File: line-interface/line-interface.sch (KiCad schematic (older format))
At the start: 25 parts

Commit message: Source transil
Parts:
- D?: footprint (none) -> Diodes_SMD:DO-214AB; Distributor (none) -> 9381830; Manufacturer (none) -> MULTICOMP; PartNo (none) -> 1.5SMCJ48CA
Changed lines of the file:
@@
 F 0 "D?" V 1154 1829 50  0000 L CNN
 F 1 "D_TVS_ALT" V 1245 1829 50  0000 L CNN
-F 2 "" H -550 350 50  0001 C CNN
+F 2 "Diodes_SMD:DO-214AB" H -550 350 50  0001 C CNN
 F 3 "" H -550 350 50  0001 C CNN
+F 4 "1.5SMCJ48CA" H 1200 1750 60  0001 C CNN "PartNo"
+F 5 "MULTICOMP" H 1200 1750 60  0001 C CNN "Manufacturer"
+F 6 "9381830" H 1200 1750 60  0001 C CNN "Distributor"
 	1    1200 1750
 	0    1    1    0

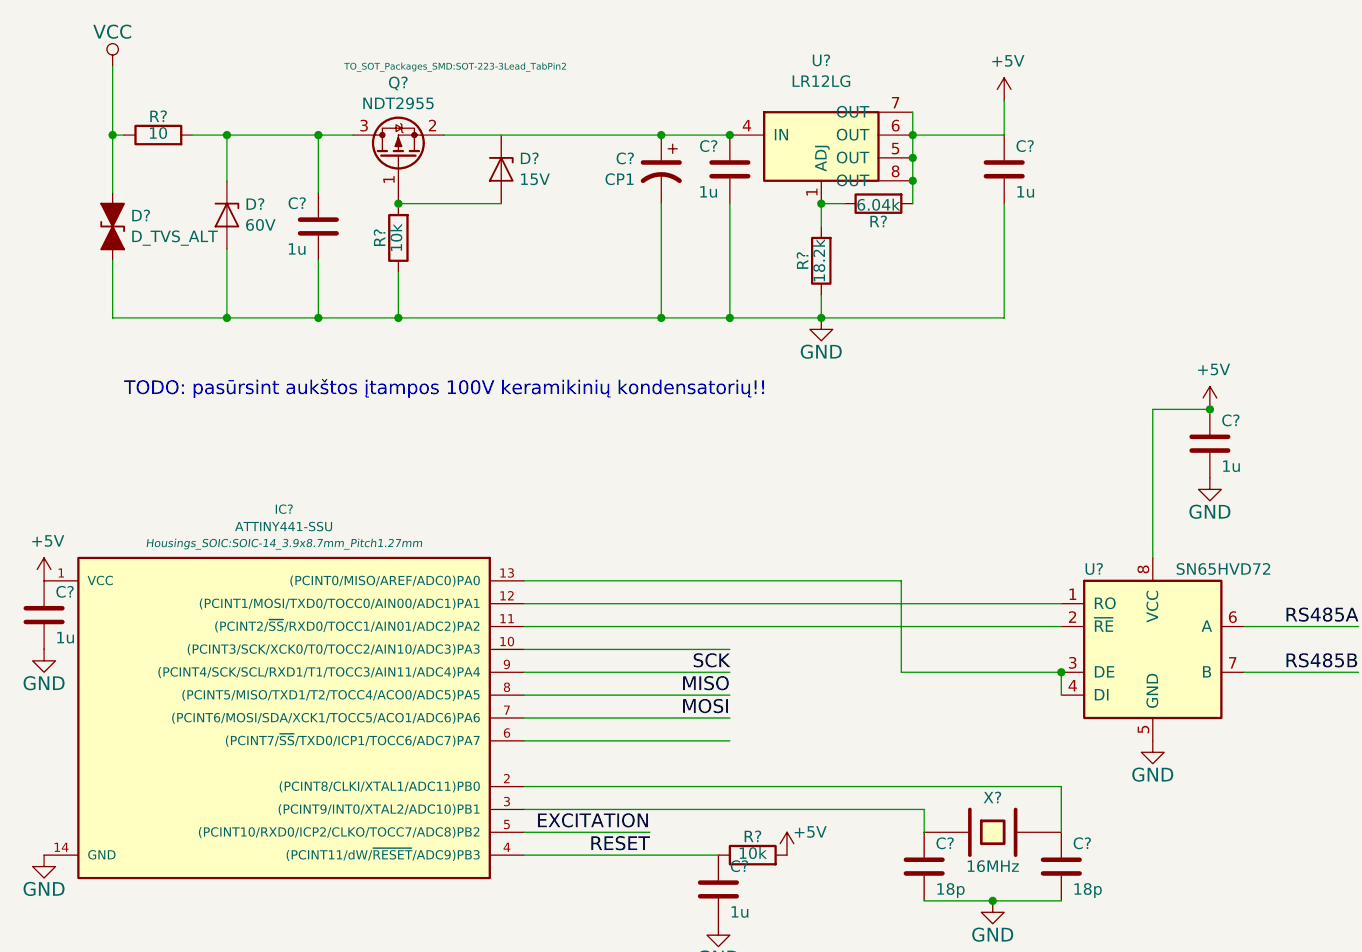
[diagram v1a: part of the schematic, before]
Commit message: Add more leds
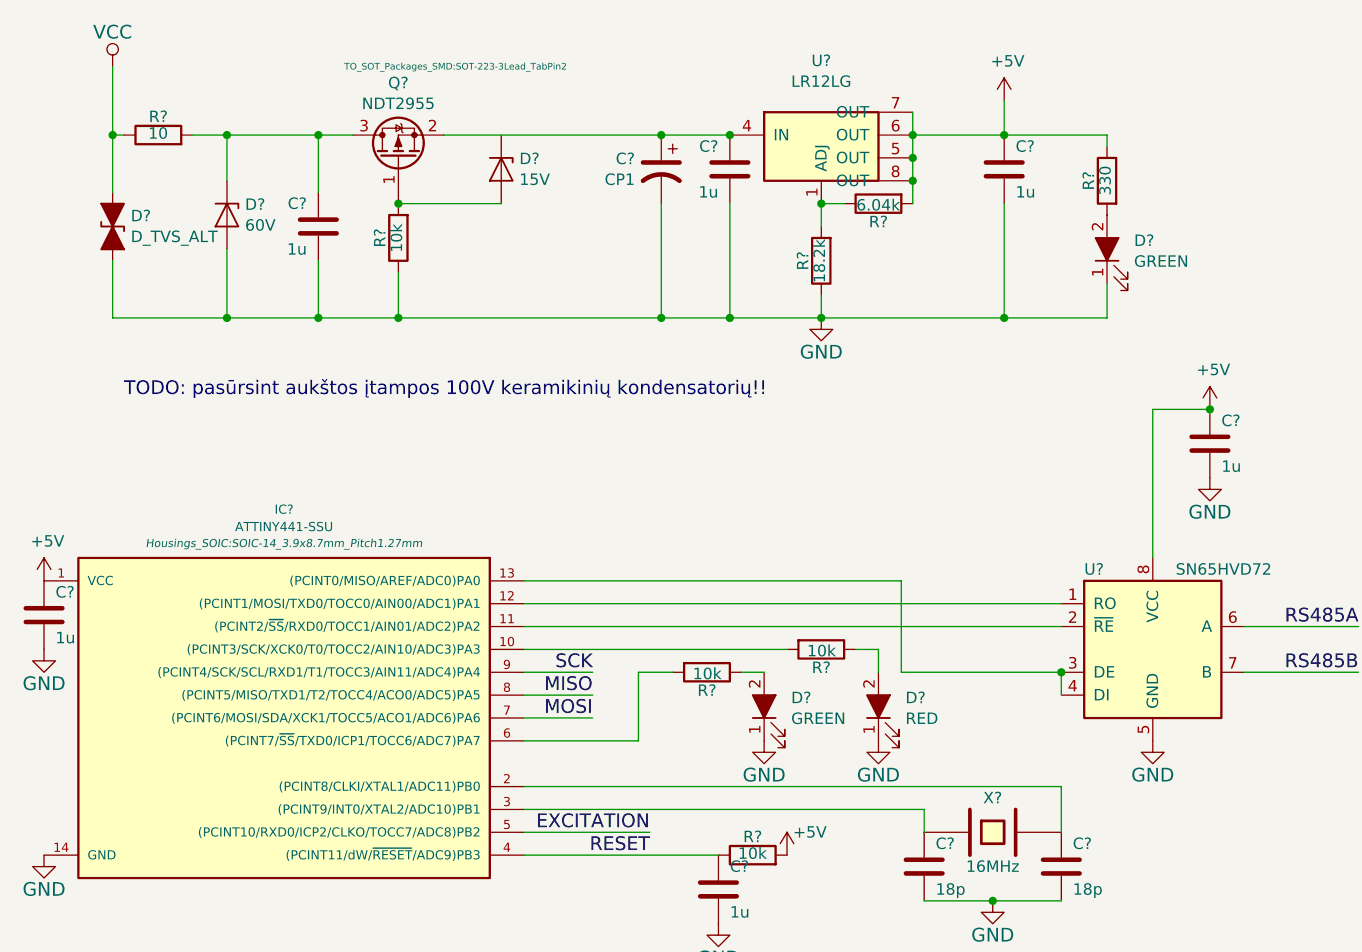
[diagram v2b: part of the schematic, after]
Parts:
- added D? (x2): GREEN, LEDs:LED_0603, symbol LED_ALT
- added D?: RED, LEDs:LED_0603, symbol LED_ALT
- added R?: 330, Resistors_SMD:R_0603, symbol R
- added R? (x2): 10k, Resistors_SMD:R_0603, symbol R
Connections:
- wire segments 57 -> 64
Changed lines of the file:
@@
 	1    0    0    -1
 $EndComp
-Text Label 3900 3700 2    60   ~ 0
+Text Label 3300 3700 2    60   ~ 0
 SCK
 Text Label 3550 4500 2    60   ~ 0
@@
 Text Label 3550 4400 2    60   ~ 0
 EXCITATION
-Text Label 3900 3800 2    60   ~ 0
+Text Label 3300 3800 2    60   ~ 0
 MISO
 Text Label 6650 3500 2    60   ~ 0
@@
 	3000 4400 3550 4400
 Wire Wire Line
-	3000 3800 3900 3800
-Wire Wire Line
-	3000 4000 3900 4000
+	3000 3800 3300 3800
+Wire Wire Line
+	3000 4000 3500 4000
 Wire Wire Line
 	6150 3500 6650 3500
@@
 	4650 3300 3000 3300
 Wire Wire Line
-	3900 3700 3000 3700
-Wire Wire Line
-	3000 3600 3900 3600
+	3300 3700 3000 3700
 $Comp
 L CONN_02X03 P?
@@
 $EndComp
 Wire Wire Line
-	4700 1350 5100 1350
+	4700 1350 5550 1350
 Connection ~ 4300 2150
 Wire Wire Line
@@
 	6150 3700 6650 3700
 Wire Wire Line
-	1200 2150 5100 2150
+	1200 2150 5550 2150
 Wire Wire Line
 	3900 1650 3900 2150
@@
 $EndComp
 Wire Wire Line
-	3000 3900 3900 3900
-Text Label 3900 3900 2    60   ~ 0
+	3000 3900 3300 3900
+Text Label 3300 3900 2    60   ~ 0
 MOSI
 $Comp
@@
 	2100 1600 2100 1350
 Connection ~ 2100 1350
+$Comp
+L LED_ALT D?
+U 1 1 58BD3E84
+P 4050 3850
+F 0 "D?" V 4088 3732 50  0000 R CNN
+F 1 "GREEN" V 3997 3732 50  0000 R CNN
+F 2 "LEDs:LED_0603" H -100 200 50  0001 C CNN
+F 3 "" H -100 200 50  0001 C CNN
+F 4 "?" H 4050 3850 60  0001 C CNN "PartNo"
+F 5 "?" H 4050 3850 60  0001 C CNN "Manufacturer"
+F 6 "?" H 4050 3850 60  0001 C CNN "Distributor"
+	1    4050 3850
+	0    -1   -1   0
+$EndComp
+$Comp
+L LED_ALT D?
+U 1 1 58BD44C6
+P 4550 3850
+F 0 "D?" V 4588 3732 50  0000 R CNN
+F 1 "RED" V 4497 3732 50  0000 R CNN
+F 2 "LEDs:LED_0603" H 400 200 50  0001 C CNN
+F 3 "" H 400 200 50  0001 C CNN
+F 4 "?" H 4550 3850 60  0001 C CNN "PartNo"
+F 5 "?" H 4550 3850 60  0001 C CNN "Manufacturer"
+F 6 "?" H 4550 3850 60  0001 C CNN "Distributor"
+	1    4550 3850
+	0    -1   -1   0
+$EndComp
+Wire Wire Line
+	4550 3600 4550 3700
+Wire Wire Line
+	3500 4000 3500 3700
+$Comp
+L GND #PWR?
+U 1 1 58BD465C
+P 4050 4000
+F 0 "#PWR?" H 4050 3750 60  0001 C CNN
+F 1 "GND" H 4050 3850 60  0000 C CNN
+F 2 "" H 4050 4000 60  0000 C CNN
+F 3 "" H 4050 4000 60  0000 C CNN
+	1    4050 4000
+	1    0    0    -1
+$EndComp
+$Comp
+L GND #PWR?
+U 1 1 58BD4709
+P 4550 4000
+F 0 "#PWR?" H 4550 3750 60  0001 C CNN
+F 1 "GND" H 4550 3850 60  0000 C CNN
+F 2 "" H 4550 4000 60  0000 C CNN
+F 3 "" H 4550 4000 60  0000 C CNN
+	1    4550 4000
+	1    0    0    -1
+$EndComp
+$Comp
+L LED_ALT D?
+U 1 1 58BD48E7
+P 5550 1850
+F 0 "D?" V 5588 1732 50  0000 R CNN
+F 1 "GREEN" V 5497 1732 50  0000 R CNN
+F 2 "LEDs:LED_0603" H 1400 -1800 50  0001 C CNN
+F 3 "" H 1400 -1800 50  0001 C CNN
+F 4 "?" H 5550 1850 60  0001 C CNN "PartNo"
+F 5 "?" H 5550 1850 60  0001 C CNN "Manufacturer"
+F 6 "?" H 5550 1850 60  0001 C CNN "Distributor"
+	1    5550 1850
+	0    -1   -1   0
+$EndComp
+Wire Wire Line
+	5550 2150 5550 2000
+Connection ~ 5100 2150
+$Comp
+L R R?
+U 1 1 58BD4C42
+P 5550 1550
+F 0 "R?" V 5630 1550 50  0000 C CNN
+F 1 "330" V 5557 1551 50  0000 C CNN
+F 2 "Resistors_SMD:R_0603" V 5480 1550 30  0001 C CNN
+F 3 "" H 5550 1550 30  0000 C CNN
+	1    5550 1550
+	-1   0    0    -1
+$EndComp
+Connection ~ 5100 1350
+Wire Wire Line
+	5550 1350 5550 1400
+$Comp
+L R R?
+U 1 1 58BD52D2
+P 4300 3600
+F 0 "R?" V 4380 3600 50  0000 C CNN
+F 1 "10k" V 4307 3601 50  0000 C CNN
+F 2 "Resistors_SMD:R_0603" V 4230 3600 30  0001 C CNN
+F 3 "" H 4300 3600 30  0000 C CNN
+	1    4300 3600
+	0    1    1    0
+$EndComp
+$Comp
+L R R?
+U 1 1 58BD5396
+P 3800 3700
+F 0 "R?" V 3880 3700 50  0000 C CNN
+F 1 "10k" V 3807 3701 50  0000 C CNN
+F 2 "Resistors_SMD:R_0603" V 3730 3700 30  0001 C CNN
+F 3 "" H 3800 3700 30  0000 C CNN
+	1    3800 3700
+	0    1    1    0
+$EndComp
+Wire Wire Line
+	3000 3600 4150 3600
+Wire Wire Line
+	4450 3600 4550 3600
+Wire Wire Line
+	3950 3700 4050 3700
+Wire Wire Line
+	3500 3700 3650 3700
 $EndSCHEMATC

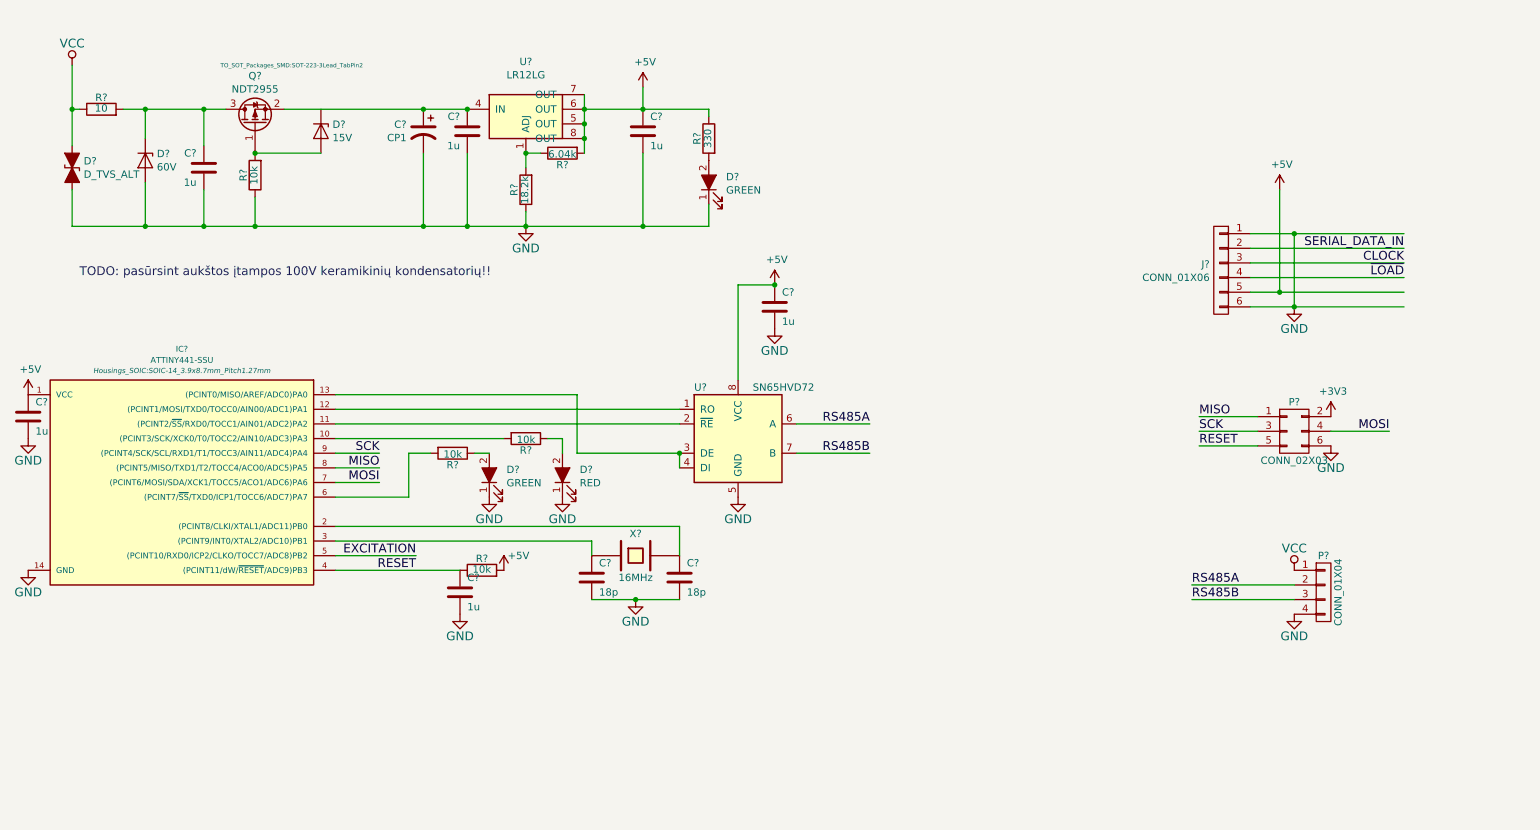
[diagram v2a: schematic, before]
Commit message: Finish sourcing the rest of components
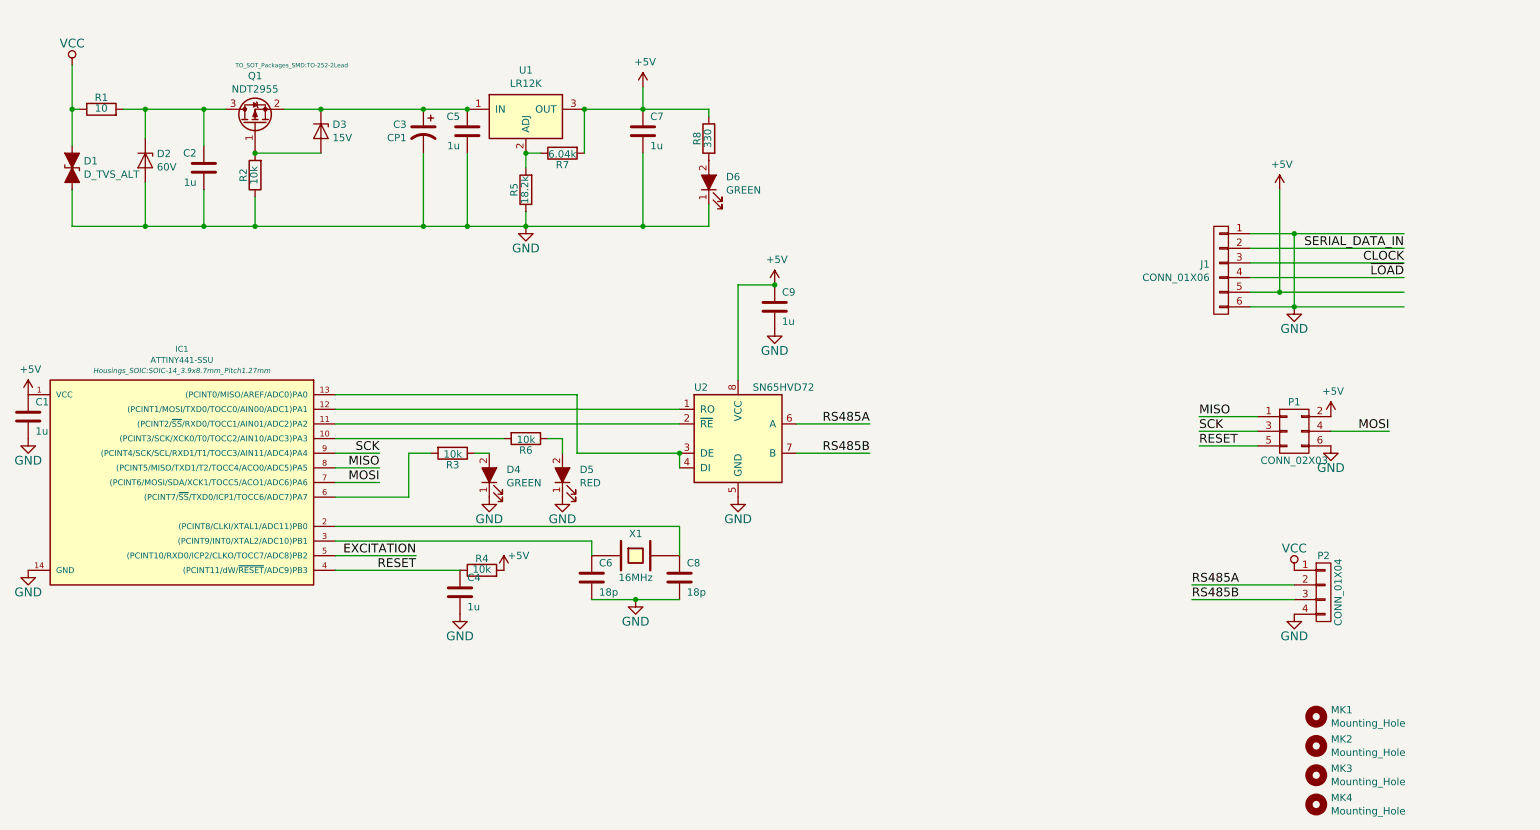
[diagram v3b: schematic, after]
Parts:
- removed U?: LR12LG, Housings_SOIC:SOIC-8_3.9x4.9mm_Pitch1.27mm, symbol LR12LG
- added MK1, MK2, MK3, MK4: Mounting_Hole, Mounting_Holes:MountingHole_3.2mm_M3, symbol Mounting_Hole
- added U1: LR12K, TO_SOT_Packages_SMD:TO-252-2Lead, symbol LR12K-RESCUE-line-interface
- C2, C5: renamed from C?; footprint Capacitors_SMD:C_0603 -> Capacitors_SMD:C_1210_HandSoldering; Distributor (none) -> 2320928; Manufacturer (none) -> ?; PartNo (none) -> ?
- C3: renamed from C?; footprint (none) -> Capacitors_ThroughHole:CP_Radial_D8.0mm_P3.50mm; Distributor (none) -> 9693939; Manufacturer (none) -> ?; PartNo (none) -> ?
- D1: renamed from D?; footprint Diodes_SMD:DO-214AB -> Diodes_SMD:Diode-SMC_Handsoldering
- D2: renamed from D?; footprint (none) -> Diodes_SMD:D_SMB_Handsoldering; Distributor (none) -> 2463618; Manufacturer (none) -> ON SEMI; PartNo (none) -> 1SMB5944BT3G
- D3: renamed from D?; footprint (none) -> Diodes_SMD:SOD-123; Distributor (none) -> 2536455; Manufacturer (none) -> ROHM; PartNo (none) -> KDZVTR15B
- J1: renamed from J?; footprint (none) -> Pin_Headers:Pin_Header_Straight_1x06_Pitch2.54mm; Distributor (none) -> ?; Manufacturer (none) -> ?; PartNo (none) -> ?
- P1: renamed from P?; footprint Pin_Headers:Pin_Header_Straight_2x03 -> Pin_Headers:Pin_Header_Straight_2x03_Pitch2.54mm; Distributor (none) -> ?; Manufacturer (none) -> ?; PartNo (none) -> ?
- Q1: renamed from Q?; footprint TO_SOT_Packages_SMD:SOT-223-3Lead_TabPin2 -> TO_SOT_Packages_SMD:TO-252-2Lead; Distributor 9846271 -> 2468040; Manufacturer (none) -> INFINEON; PartNo ? -> IRFR5410TRPBF
- R1: renamed from R?; Distributor ? -> 1738932
- R5: renamed from R?; footprint Resistors_SMD:R_0603 -> Resistors_SMD:R_0603_HandSoldering; Distributor (none) -> 1469829; Manufacturer (none) -> ?; PartNo (none) -> ?
- R7: renamed from R?; footprint Resistors_SMD:R_0603 -> Resistors_SMD:R_0603_HandSoldering; Distributor (none) -> 2059386; Manufacturer (none) -> ?; PartNo (none) -> ?
- gave numbers to parts that had none: 18
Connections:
- net labels removed: +3V3
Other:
- note removed: "TODO: pasūrsint aukštos įtampos 100V keramikinių kondensatorių!!"

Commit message: Add resistors to SPI lines, hook up to the connector
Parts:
- added D7: D, Diodes_SMD:D_SOD-123, symbol D
- added R10, R9: 10k, Resistors_SMD:R_0603, symbol R
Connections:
- net labels added: ~CS
- wire segments 64 -> 68
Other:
- moved on the sheet: C6, C8, C9, D5, R3, U2, X1
